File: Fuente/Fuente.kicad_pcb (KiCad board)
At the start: 2 copper layers, 16 parts, among them J1 USB_B_Mini, J2 Conn_01x02_Pin, J3 Conn_01x02_Pin, U2 LM1117DT-3.3, U3 TPS61087DSCR

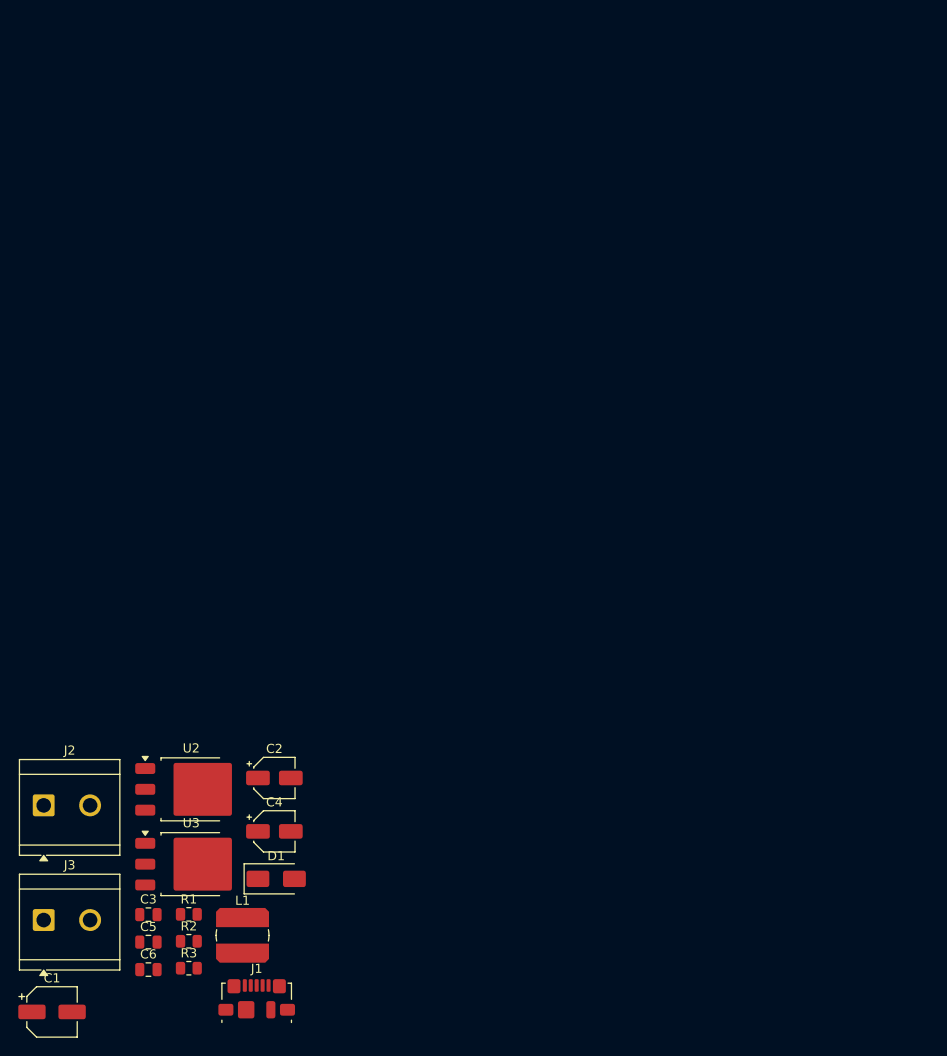
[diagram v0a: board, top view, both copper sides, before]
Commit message: Incorporación de agujeros de montaje y acomodo del diseño de la PCB
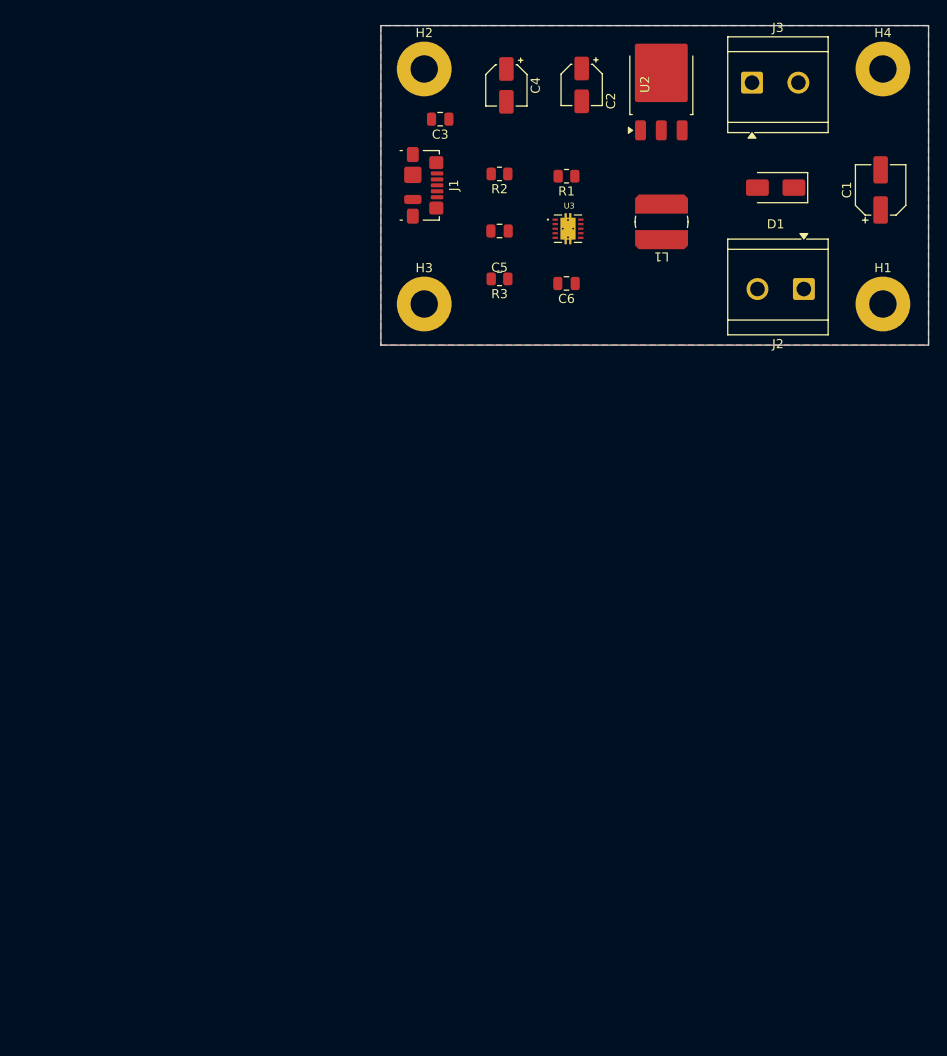
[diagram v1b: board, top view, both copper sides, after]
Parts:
- added H1: MountingHole_Pad_MP, MountingHole:MountingHole_3mm_Pad, F.Cu at (187.8, 93.5)
- added H2: MountingHole_Pad_MP, MountingHole:MountingHole_3mm_Pad, F.Cu at (137.5, 67.8)
- added H3: MountingHole_Pad_MP, MountingHole:MountingHole_3mm_Pad, F.Cu at (137.5, 93.5)
- added H4: MountingHole_Pad_MP, MountingHole:MountingHole_3mm_Pad, F.Cu at (187.8, 67.8)
- U3: footprint Package_TO_SOT_SMD:TO-252-3_TabPin2 -> TPS61087DRC:IC_TPS61087DSCR
- moved C1 127.9 mm to (187.5, 81.0), turned to 90 degrees
- moved J3 120.2 mm to (173.4, 69.2)
- moved J2 100.7 mm to (179.1, 91.9), turned to 180 degrees
- moved D1 93.4 mm to (176.0, 80.8), turned to 180 degrees
- moved U2 92.8 mm to (163.5, 69.4), turned to 90 degrees
- moved C3 92.8 mm to (139.2, 73.2), turned to 180 degrees
- moved J1 91.0 mm to (137.4, 80.5), turned to -90 degrees
- moved R1 90.8 mm to (153.1, 79.5), turned to 180 degrees
- moved R2 90.7 mm to (145.8, 79.2), turned to 180 degrees
- moved L1 90.6 mm to (163.5, 84.5), turned to 180 degrees
- moved C6 88.0 mm to (153.1, 91.2), turned to 180 degrees
- moved C5 86.9 mm to (145.8, 85.5), turned to 180 degrees
- moved C4 85.6 mm to (146.5, 69.5), turned to -90 degrees
- moved C2 83.1 mm to (154.8, 69.5), turned to -90 degrees
- moved R3 82.8 mm to (145.8, 90.8), turned to 180 degrees
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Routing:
- added copper zone on F.Cu, net +5v
- added copper zone on B.Cu, net GND
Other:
- board outline added: 60 x 35 mm

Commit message: Diseño completado v0.1
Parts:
- moved C6 8.03 mm to (153.8, 83.2)
- moved U3 4.06 mm to (153.9, 89.2)
- moved U2 1.03 mm to (163.5, 70.5)
- moved R1 0.72 mm to (153.8, 79.2)
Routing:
- net +12V: track 0.00 -> 84.9 mm
- net +5v: track 0.00 -> 62.2 mm
- net /FB: track 0.00 -> 31.3 mm
- net +3.3v: track 0.00 -> 26.7 mm
- net Net-(D1-A): track 0.00 -> 23.4 mm
- net GND: track 0.00 -> 19.7 mm
- net Net-(U3-COMP): track 0.00 -> 6.90 mm
- net Net-(C5-Pad1): track 0.00 -> 6.02 mm
- net Net-(U3-SS): track 0.00 -> 5.25 mm
- added copper zone on F.Cu, net GND
- removed copper zone on F.Cu, net +5v

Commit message: Versión mejorada con agujeros pasantes
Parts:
- J2, J3: footprint TerminalBlock_CUI:TerminalBlock_CUI_TB007-508-02_1x02_P5.08mm_Horizontal -> TerminalBlock_Phoenix:TerminalBlock_Phoenix_MKDS-1,5-2_1x02_P5.00mm_Horizontal
- moved J2 5.59 mm to (173.5, 91.7), turned to 0 degrees
- moved J3 5.09 mm to (178.5, 69.2), turned to 180 degrees
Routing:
- net +12V: track 84.9 -> 49.4 mm, vias 0 -> 2
- net +5v: track 62.2 -> 71.4 mm, vias 0 -> 2
- net +3.3v: track 26.7 -> 34.3 mm
- net GND: track 19.7 -> 14.1 mm

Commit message: Creación e incorporación de Lógotipo UAA
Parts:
- added Log1: LOGO, IE UAA:IE UAA, F.Cu at (162.5, 93.5)
